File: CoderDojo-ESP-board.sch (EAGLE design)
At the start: 7 parts, among them IC1 ESP-12E/F, IC2 FT232RL

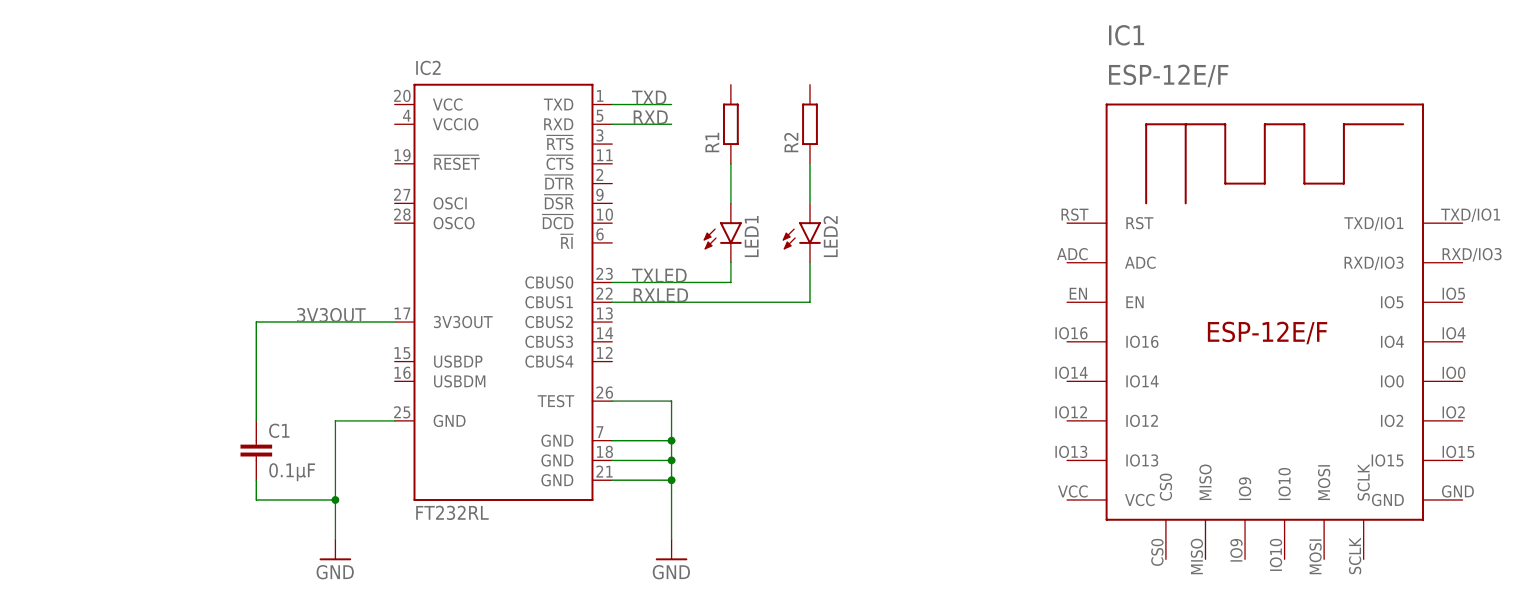
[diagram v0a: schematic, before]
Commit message: Add FT232RL to schematic
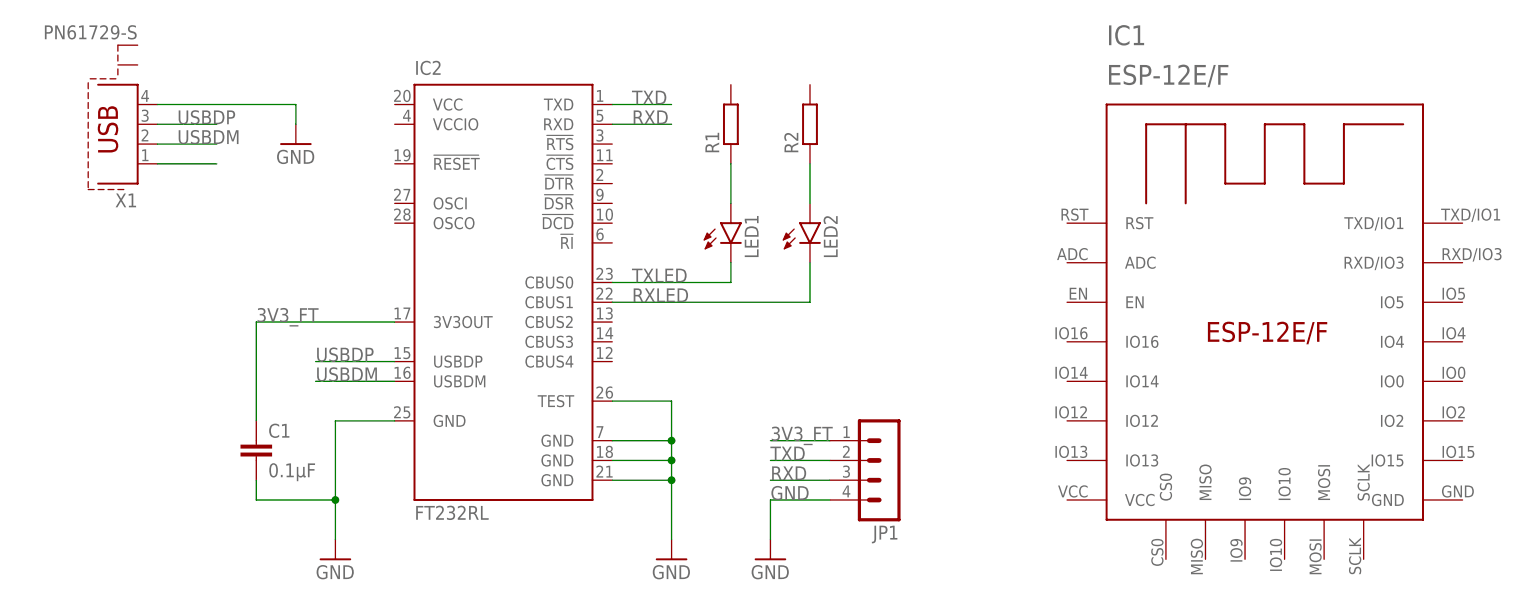
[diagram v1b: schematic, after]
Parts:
- added JP1: (no value), con-lstb:MA04-1
- added X1: PN61729-S, con-berg:PN61729-S
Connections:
- removed net 3V3OUT: C1.1, IC2.3V3OUT
- new net 3V3_FT: C1.1, IC2.3V3OUT, JP1.1
- new net N$3: X1.1
- new net USBDM: IC2.USBDM, X1.2
- new net USBDP: IC2.USBDP, X1.3
- net GND: now also JP1.4, X1.4
- net RXD: now also JP1.3
- net TXD: now also JP1.2
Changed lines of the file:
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@@
 <part name="R1" library="rcl" library_urn="urn:adsk.eagle:library:334" deviceset="R-EU_" device="R0805" package3d_urn="urn:adsk.eagle:package:23553/2"/>
 <part name="R2" library="rcl" library_urn="urn:adsk.eagle:library:334" deviceset="R-EU_" device="R0805" package3d_urn="urn:adsk.eagle:package:23553/2"/>
+<part name="JP1" library="con-lstb" library_urn="urn:adsk.eagle:library:162" deviceset="MA04-1" device="" package3d_urn="urn:adsk.eagle:package:8337/1"/>
+<part name="GND3" library="supply1" library_urn="urn:adsk.eagle:library:371" deviceset="GND" device=""/>
+<part name="X1" library="con-berg" library_urn="urn:adsk.eagle:library:130" deviceset="PN61729-S" device="" package3d_urn="urn:adsk.eagle:package:6149/1"/>
+<part name="GND4" library="supply1" library_urn="urn:adsk.eagle:library:371" deviceset="GND" device=""/>
 </parts>
 <sheets>
@@
 <attribute name="NAME" x="105.1814" y="67.31" size="1.778" layer="95" rot="R90"/>
 <attribute name="VALUE" x="109.982" y="67.31" size="1.778" layer="96" rot="R90"/>
+</instance>
+<instance part="JP1" gate="1" x="116.84" y="25.4" smashed="yes" rot="R180">
+<attribute name="VALUE" x="118.11" y="35.56" size="1.778" layer="96" rot="R180"/>
+<attribute name="NAME" x="118.11" y="19.558" size="1.778" layer="95" rot="R180"/>
+</instance>
+<instance part="GND3" gate="1" x="101.6" y="15.24" smashed="yes">
+<attribute name="VALUE" x="99.06" y="12.7" size="1.778" layer="96"/>
+</instance>
+<instance part="X1" gate="G$1" x="20.32" y="71.12" smashed="yes" rot="R180">
+<attribute name="NAME" x="20.32" y="62.23" size="1.778" layer="95" rot="R180"/>
+<attribute name="VALUE" x="20.32" y="83.82" size="1.778" layer="96" rot="R180"/>
+</instance>
+<instance part="GND4" gate="1" x="40.64" y="68.58" smashed="yes">
+<attribute name="VALUE" x="38.1" y="66.04" size="1.778" layer="96"/>
 </instance>
 </instances>
@@
 <junction x="88.9" y="30.48"/>
 </segment>
+<segment>
+<pinref part="JP1" gate="1" pin="4"/>
+<wire x1="109.22" y1="22.86" x2="101.6" y2="22.86" width="0.1524" layer="91"/>
+<pinref part="GND3" gate="1" pin="GND"/>
+<wire x1="101.6" y1="22.86" x2="101.6" y2="17.78" width="0.1524" layer="91"/>
+<label x="101.6" y="22.86" size="1.778" layer="95"/>
+</segment>
+<segment>
+<pinref part="X1" gate="G$1" pin="4"/>
+<pinref part="GND4" gate="1" pin="GND"/>
+<wire x1="22.86" y1="73.66" x2="40.64" y2="73.66" width="0.1524" layer="91"/>
+<wire x1="40.64" y1="73.66" x2="40.64" y2="71.12" width="0.1524" layer="91"/>
+</segment>
 </net>
 <net name="TXD" class="0">
@@
 <label x="83.82" y="73.66" size="1.778" layer="95"/>
 </segment>
+<segment>
+<pinref part="JP1" gate="1" pin="2"/>
+<wire x1="109.22" y1="27.94" x2="101.6" y2="27.94" width="0.1524" layer="91"/>
+<label x="101.6" y="27.94" size="1.778" layer="95"/>
+</segment>
 </net>
 <net name="RXD" class="0">
@@
 <label x="83.82" y="71.12" size="1.778" layer="95"/>
 </segment>
-</net>
-<net name="3V3OUT" class="0">
+<segment>
+<pinref part="JP1" gate="1" pin="3"/>
+<wire x1="109.22" y1="25.4" x2="101.6" y2="25.4" width="0.1524" layer="91"/>
+<label x="101.6" y="25.4" size="1.778" layer="95"/>
+</segment>
+</net>
+<net name="3V3_FT" class="0">
 <segment>
 <pinref part="IC2" gate="1" pin="3V3OUT"/>
@@
 <wire x1="53.34" y1="45.72" x2="35.56" y2="45.72" width="0.1524" layer="91"/>
 <wire x1="35.56" y1="45.72" x2="35.56" y2="33.02" width="0.1524" layer="91"/>
-<label x="40.64" y="45.72" size="1.778" layer="95"/>
+<label x="35.56" y="45.72" size="1.778" layer="95"/>
+</segment>
+<segment>
+<pinref part="JP1" gate="1" pin="1"/>
+<wire x1="109.22" y1="30.48" x2="101.6" y2="30.48" width="0.1524" layer="91"/>
+<label x="101.6" y="30.48" size="1.778" layer="95"/>
 </segment>
 </net>
@@
 </segment>
 </net>
+<net name="N$3" class="0">
+<segment>
+<pinref part="X1" gate="G$1" pin="1"/>
+<wire x1="22.86" y1="66.04" x2="30.48" y2="66.04" width="0.1524" layer="91"/>
+</segment>
+</net>
+<net name="USBDM" class="0">
+<segment>
+<pinref part="X1" gate="G$1" pin="2"/>
+<wire x1="22.86" y1="68.58" x2="30.48" y2="68.58" width="0.1524" layer="91"/>
+<label x="25.4" y="68.58" size="1.778" layer="95"/>
+</segment>
+<segment>
+<pinref part="IC2" gate="1" pin="USBDM"/>
+<wire x1="53.34" y1="38.1" x2="43.18" y2="38.1" width="0.1524" layer="91"/>
+<label x="43.18" y="38.1" size="1.778" layer="95"/>
+</segment>
+</net>
+<net name="USBDP" class="0">
+<segment>
+<pinref part="X1" gate="G$1" pin="3"/>
+<wire x1="22.86" y1="71.12" x2="30.48" y2="71.12" width="0.1524" layer="91"/>
+<label x="25.4" y="71.12" size="1.778" layer="95"/>
+</segment>
+<segment>
+<pinref part="IC2" gate="1" pin="USBDP"/>
+<wire x1="53.34" y1="40.64" x2="43.18" y2="40.64" width="0.1524" layer="91"/>
+<label x="43.18" y="40.64" size="1.778" layer="95"/>
+</segment>
+</net>
